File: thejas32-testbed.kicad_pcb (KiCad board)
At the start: 4 copper layers, 141.5 x 110 mm, 98 parts, among them J1 Conn_02x04_Odd_Even, J10 Conn_02x10_Odd_Even, J11 Conn_02x03_Odd_Even, J12 Conn_02x20_Odd_Even, J13 Conn_02x06_Odd_Even, J2 USB_B_Micro, J3 Conn_02x03_Odd_Even, J4 Conn_02x04_Odd_Even, J6 Conn_02x06_Odd_Even, J7 Conn_01x05, U1 Pico Master, U2 THEJAS32, U3 Pico Slave, U6 W25Q16JVSSIQ

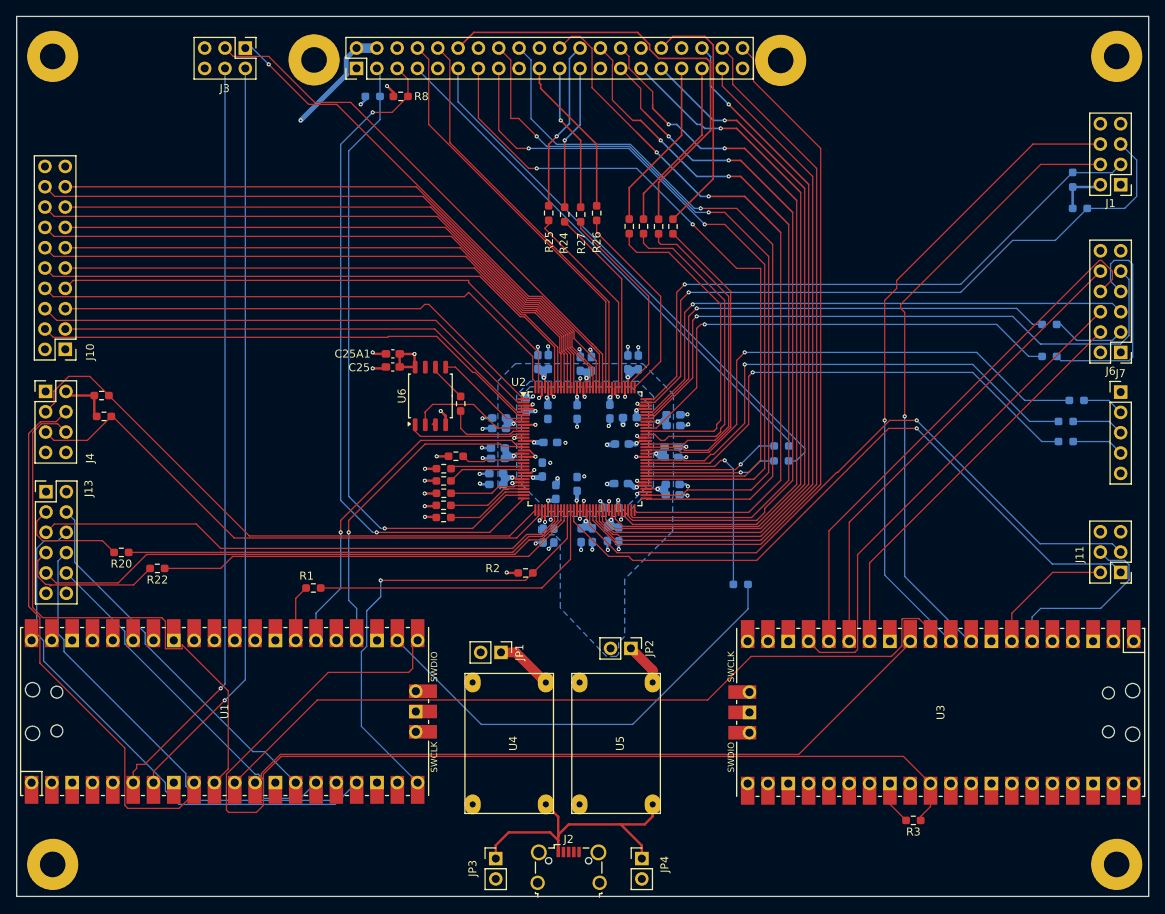
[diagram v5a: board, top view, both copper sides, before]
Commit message: Nicely routed PCB, clean lines
Reasonable spacing between traces. Could be improved.
Done for testing mostly.
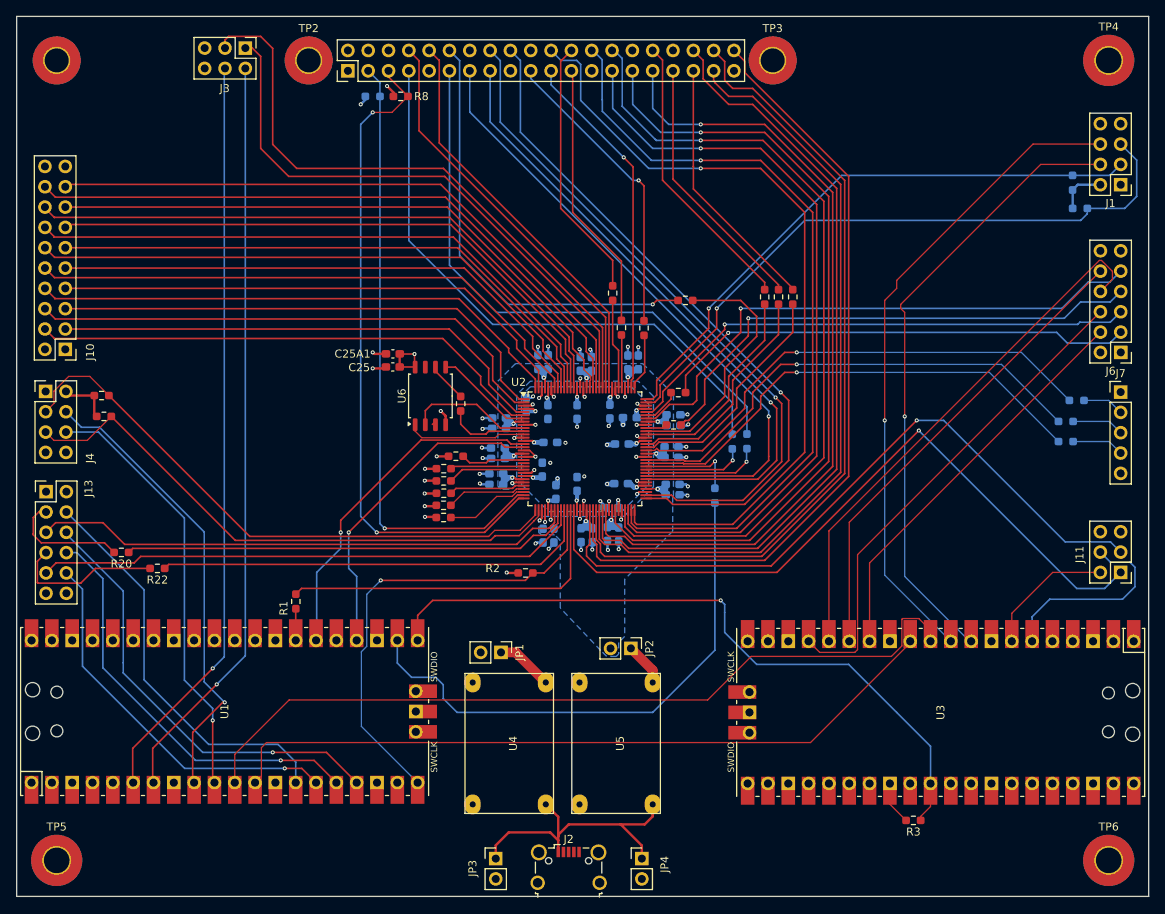
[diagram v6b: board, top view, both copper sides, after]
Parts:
- removed R27: 0E, project_lib:proj_R_0603_1608Metric_Pad0.98x0.95mm_HandSolder
- R16, R18: moved to F.Cu
- TP1, TP2, TP3: footprint MountingHole:MountingHole_3.2mm_M3_Pad -> MountingHole:MountingHole_3mm_Pad_TopBottom
- TP4, TP5, TP6: footprint MountingHole:MountingHole_3.2mm_M3_Pad -> MountingHole:MountingHole_3.2mm_M3_Pad_TopBottom
- moved TP1 166.3 mm to (89.5, 55.5)
- moved TP6 108.1 mm to (221.0, 155.5)
- moved TP2 105.5 mm to (121.0, 55.5)
- moved TP5 105.1 mm to (89.5, 155.5)
- moved TP3 90.0 mm to (179.0, 55.5)
- moved R18 47.7 mm to (166.6, 101.1)
- moved R16 47.2 mm to (167.2, 97.0)
- moved R29 17.5 mm to (178.0, 85.1)
- moved R30 17.4 mm to (179.7, 85.1)
- moved R31 17.4 mm to (181.5, 85.1)
- moved R24 15.8 mm to (160.1, 88.9)
- moved R26 15.5 mm to (162.9, 89.0)
- moved R25 12.8 mm to (159.0, 84.6)
- moved R28 11.6 mm to (168.1, 85.5), turned to 180 degrees
- moved R35 11.6 mm to (171.8, 109.9), turned to -90 degrees
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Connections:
- R28 pad 2: RPi_COMPAT_PWM1 -> RPi_COMPAT_PWM0
- R29 pad 2: RPi_COMPAT_PWM1_ALT -> RPi_COMPAT_PWM0_ALT
- R30 pad 2: RPi_COMPAT_PWM0 -> RPi_COMPAT_PWM1
- R31 pad 2: RPi_COMPAT_PWM0_ALT -> RPi_COMPAT_PWM1_ALT
- U2 pad 98: Net-(U2-SPI2_MISO) -> RPi_COMPAT_SPI0_MISO
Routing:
- net Net-(U2-SPI0_MOSI): track 60.8 -> 2.67 mm, vias 1 -> 0
- net Net-(U2-SPIO0_CLK): track 60.4 -> 4.76 mm, vias 1 -> 0
- net Net-(J6-Pin_3): track 9.27 -> 59.9 mm, vias 0 -> 1
- net PICO_SLAVE_RUN: track 136.8 -> 87.4 mm, vias 0 -> 1
- net Net-(J6-Pin_7): track 28.6 -> 65.0 mm, vias 0 -> 1
- net RPi_COMPAT_SPI0_MISO: track 18.4 -> 44.7 mm
- net Net-(U2-SPI2_MISO): track 25.1 -> 0.00 mm
- net Net-(U2-SPI2_MOSI): track 26.1 -> 8.31 mm
- net RPi_COMPAT_SPI0_MOSI: track 20.1 -> 37.5 mm, vias 0 -> 1
- net Net-(U2-SPI2_CLK): track 23.7 -> 6.58 mm
- net MCU_I2C0_SDA: track 70.6 -> 53.9 mm, vias 0 -> 1
- net RPi_COMPAT_SPI0_SCLK: track 18.1 -> 33.8 mm, vias 1 -> 0
- net Net-(U2-PWM1): track 41.0 -> 25.9 mm
- net Net-(U2-PWM7): track 26.1 -> 12.2 mm
- net Net-(U2-SPI2_CSN): track 24.9 -> 11.2 mm
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
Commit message: Single pico, new layout
Figured two picos was too much as a concept. So, simplify.

Reduce number of jumpers etc also (especially in passthrough).

The single pico breaks out pins conveniently for users for
usage.
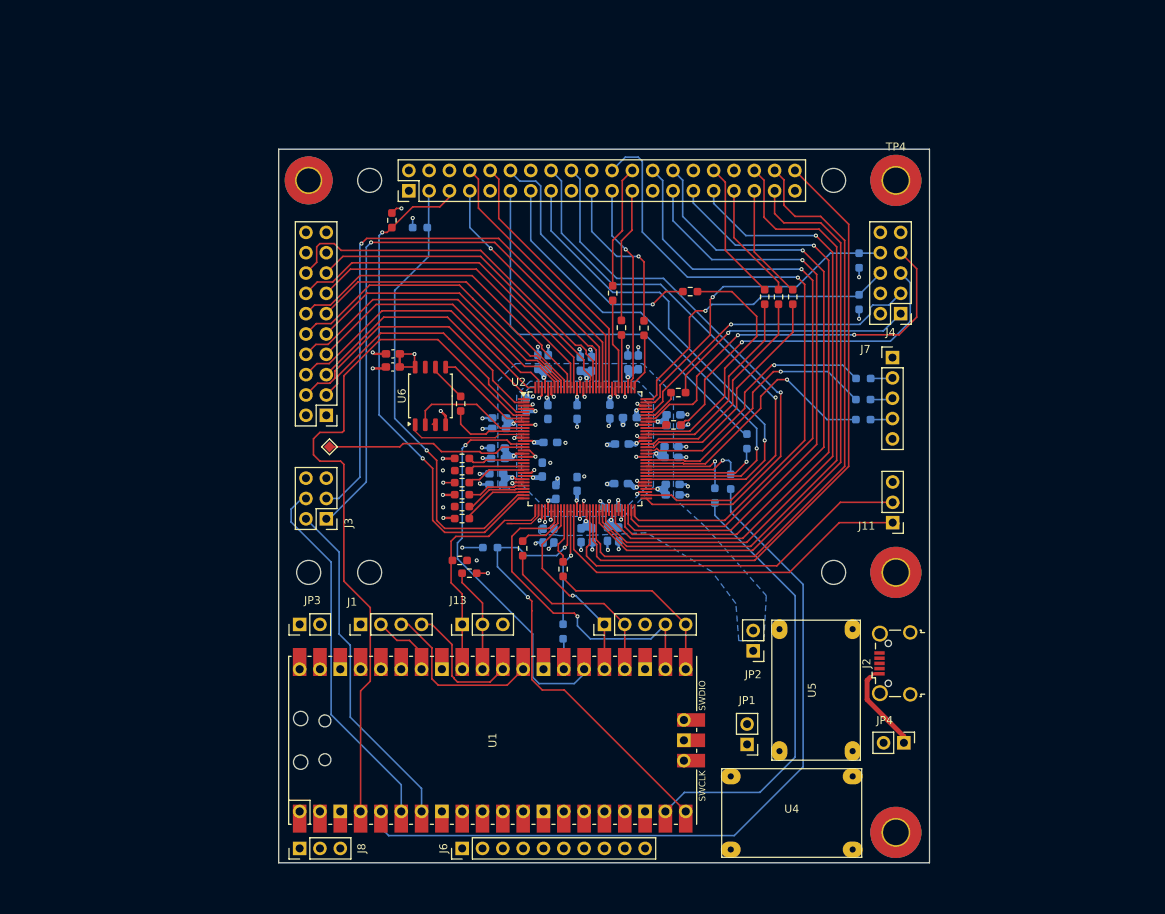
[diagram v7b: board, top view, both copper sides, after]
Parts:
- removed R3: 10K, project_lib:proj_R_0603_1608Metric_Pad0.98x0.95mm_HandSolder
- removed TP3: Mounting Hole, MountingHole:MountingHole_3mm_Pad_TopBottom
- removed TP5: Mounting Hole, MountingHole:MountingHole_3.2mm_M3_Pad_TopBottom
- removed U3: Pico Slave, RPi_Pico:RPi_Pico_SMD_TH
- added H1: MountingHole, MountingHole:MountingHole_3mm, F.Cu at (128.6, 70.5)
- added H2: MountingHole, MountingHole:MountingHole_3mm, F.Cu at (186.6, 70.5)
- added H3: MountingHole, MountingHole:MountingHole_3mm, F.Cu at (128.6, 119.5)
- added H4: MountingHole, MountingHole:MountingHole_3mm, F.Cu at (186.6, 119.5)
- added H5: MountingHole, MountingHole:MountingHole_3mm, F.Cu at (121.0, 119.5)
- added J8: Conn_01x03, Connector_PinHeader_2.54mm:PinHeader_1x03_P2.54mm_Vertical, F.Cu at (119.9, 154.0)
- added J9: Conn_01x05, Connector_PinHeader_2.54mm:PinHeader_1x05_P2.54mm_Vertical, F.Cu at (158.0, 126.0)
- added TP7: TestPoint, TestPoint:TestPoint_Pad_1.0x1.0mm, F.Cu at (123.6, 103.8)
- J1: value Conn_02x04_Odd_Even -> Conn_01x04; footprint Connector_PinHeader_2.54mm:PinHeader_2x04_P2.54mm_Vertical -> Connector_PinHeader_2.54mm:PinHeader_1x04_P2.54mm_Vertical
- J11: value Conn_02x03_Odd_Even -> Conn_01x03; footprint Connector_PinHeader_2.54mm:PinHeader_2x03_P2.54mm_Vertical -> Connector_PinHeader_2.54mm:PinHeader_1x03_P2.54mm_Vertical
- J13: value Conn_02x06_Odd_Even -> Conn_01x03; footprint Connector_PinHeader_2.54mm:PinHeader_2x06_P2.54mm_Vertical -> Connector_PinHeader_2.54mm:PinHeader_1x03_P2.54mm_Vertical
- J4: value Conn_02x04_Odd_Even -> Conn_02x05_Odd_Even; footprint Connector_PinHeader_2.54mm:PinHeader_2x04_P2.54mm_Vertical -> Connector_PinHeader_2.54mm:PinHeader_2x05_P2.54mm_Vertical
- J6: value Conn_02x06_Odd_Even -> Conn_01x10; footprint Connector_PinHeader_2.54mm:PinHeader_2x06_P2.54mm_Vertical -> Connector_PinHeader_2.54mm:PinHeader_1x10_P2.54mm_Vertical
- R1, R2: moved to B.Cu
- TP2: footprint MountingHole:MountingHole_3mm_Pad_TopBottom -> MountingHole:MountingHole_3.2mm_M3_Pad_TopBottom
- moved TP2 121.2 mm to (194.4, 152.0)
- moved J1 109.8 mm to (127.5, 126.0), turned to 90 degrees
- moved J4 107.3 mm to (195.0, 87.2), turned to 180 degrees
- moved J6 103.1 mm to (140.2, 154.0), turned to 90 degrees
- moved J3 59.7 mm to (123.2, 112.8), turned to 180 degrees
- moved J13 54.6 mm to (140.2, 126.0), turned to 90 degrees
- moved R22 50.7 mm to (152.8, 119.1), turned to -90 degrees
- moved R20 50.2 mm to (147.8, 116.5), turned to -90 degrees
- moved R5 49.7 mm to (141.1, 119.6), turned to 180 degrees
- moved R4 49.3 mm to (139.9, 118.0), turned to 180 degrees
- moved J2 48.1 mm to (194.2, 130.9), turned to 90 degrees
- moved TP6 44.8 mm to (194.4, 119.5)
- moved JP3 38.2 mm to (119.9, 126.0), turned to 90 degrees
- moved U4 36.4 mm to (181.4, 149.6), turned to 180 degrees
- moved JP4 35.8 mm to (195.4, 140.8), turned to -90 degrees
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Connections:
- J1 pad 1: PWR_3V3 -> GND
- J1 pad 2: PWR_3V3 -> Net-(J1-Pin_2)
- J1 pad 4: MCU_I2C1_SCL -> Net-(J1-Pin_4)
- J10 pad 10: MCU_GPIO_22 -> MCU_GPIO_24
- J10 pad 12: MCU_GPIO_24 -> MCU_GPIO_26
- J10 pad 14: MCU_GPIO_26 -> MCU_GPIO_28
- J10 pad 16: MCU_GPIO_28 -> MCU_GPIO_30
- J10 pad 17: MCU_GPIO_31 -> unconnected-(J10-Pin_17-Pad17)
- J10 pad 18: MCU_GPIO_30 -> unconnected-(J10-Pin_18-Pad18)
- J10 pad 4: MCU_GPIO_16 -> MCU_GPIO_18
- J10 pad 6: MCU_GPIO_18 -> MCU_GPIO_20
- J10 pad 8: MCU_GPIO_20 -> MCU_GPIO_22
- J11 pad 2: MCU_UART1_TX -> Net-(J11-Pin_2)
- J11 pad 3: Net-(J11-Pin_3) -> GND
- J13 pad 1: PWR_3V3 -> MCU_I2C0_SCL
- J13 pad 2: PWR_3V3 -> MCU_I2C0_SDA
- J13 pad 3: Net-(J13-Pin_3) -> GND
- J2 pad 1: PWR_5V -> Net-(J2-VBUS)
- J4 pad 1: PWR_3V3 -> MCU_SPI0_SCK
- J4 pad 3: Net-(J4-Pin_3) -> MCU_SPI0_CSN
- J4 pad 4: MCU_I2C0_SCL -> PWR_3V3
- J4 pad 5: Net-(J4-Pin_5) -> MCU_SPI0_MOSI
- J4 pad 6: MCU_I2C0_SDA -> MCU_I2C1_SCL
- J4 pad 7: GND -> MCU_SPI0_MISO
- J4 pad 8: GND -> MCU_I2C1_SDA
- J6 pad 1: PWR_3V3 -> Net-(J6-Pin_1)
- J6 pad 10: MCU_SPI0_MISO -> GND
- J6 pad 2: PWR_3V3 -> Net-(J6-Pin_2)
- J6 pad 4: MCU_SPI0_SCK -> Net-(J6-Pin_4)
- J6 pad 5: Net-(J6-Pin_5) -> GND
- J6 pad 6: MCU_SPI0_CSN -> Net-(J6-Pin_6)
- J6 pad 8: MCU_SPI0_MOSI -> Net-(J6-Pin_8)
- JP4 pad 1: PWR_5V -> Net-(J2-VBUS)
- JP4 pad 2: Net-(JP4-B) -> PWR_5V
- R16 pad 2: Net-(J6-Pin_3) -> MCU_SPI0_SCK
- R18 pad 2: Net-(J6-Pin_7) -> MCU_SPI0_MOSI
- R20 pad 2: Net-(J13-Pin_3) -> MCU_SPI1_SCK
- R22 pad 2: Net-(J13-Pin_7) -> MCU_SPI1_MOSI
- R36 pad 2: RPi_COMPAT_GPIO_4 -> MCU_GPIO_00
- R4 pad 2: Net-(J4-Pin_3) -> MCU_I2C0_SCL
- R5 pad 2: Net-(J4-Pin_5) -> MCU_I2C0_SDA
- R6 pad 2: Net-(J1-Pin_3) -> MCU_I2C1_SCL
- R7 pad 2: Net-(J1-Pin_5) -> MCU_I2C1_SDA
- U1 pad 1: unconnected-(U1-GPIO0-Pad1)_0 -> Net-(J8-Pin_1)
- U1 pad 10: MCU_I2C0_SDA -> Net-(J6-Pin_2)
- U1 pad 11: PICO_COMM_1 -> Net-(J6-Pin_3)
- U1 pad 12: PICO_COMM_2 -> Net-(J6-Pin_4)
- U1 pad 14: MCU_SPI1_SCK -> Net-(J6-Pin_6)
- U1 pad 15: MCU_SPI1_MISO -> Net-(J6-Pin_7)
- U1 pad 16: MCU_SPI1_MOSI -> Net-(J6-Pin_8)
- U1 pad 17: MCU_SPI1_CSN -> Net-(J6-Pin_9)
- U1 pad 19: unconnected-(U1-GPIO14-Pad19)_0 -> MCU_PWM_7
- U1 pad 2: unconnected-(U1-GPIO1-Pad2) -> Net-(J8-Pin_2)
- U1 pad 21: PICO_SLAVE_RUN -> MCU_SPI1_MOSI
- U1 pad 22: MCU_PWM_7 -> MCU_SPI1_CSN
- U1 pad 24: MCU_HEART_BEAT -> MCU_SPI1_SCK
- U1 pad 25: unconnected-(U1-GPIO19-Pad25) -> MCU_SPI1_MISO
- U1 pad 29: unconnected-(U1-GPIO22-Pad29) -> Net-(J1-Pin_3)
- U1 pad 30: unconnected-(U1-RUN-Pad30) -> Net-(J1-Pin_4)
- U1 pad 31: unconnected-(U1-GPIO26_ADC0-Pad31)_0 -> MCU_I2C0_SDA
- U1 pad 32: unconnected-(U1-GPIO27_ADC1-Pad32)_0 -> MCU_I2C0_SCL
- U1 pad 34: unconnected-(U1-GPIO28_ADC2-Pad34)_0 -> Net-(J1-Pin_2)
- U1 pad 4: unconnected-(U1-GPIO2-Pad4)_0 -> MCU_GPIO_16
- U1 pad 5: unconnected-(U1-GPIO3-Pad5) -> MCU_GPIO_00
- U1 pad 9: MCU_I2C0_SCL -> Net-(J6-Pin_1)
- U2 pad 109: MCU_GPIO_31 -> RPi_COMPAT_GPIO_4
- U2 pad 16: MCU_HEART_BEAT -> Net-(U2-PROC_HEART_BEAT)
- U2 pad 33: Net-(J4-Pin_3) -> MCU_I2C0_SCL
- U2 pad 34: Net-(J4-Pin_5) -> MCU_I2C0_SDA
- U2 pad 39: Net-(J13-Pin_5) -> MCU_SPI1_CSN
- U2 pad 41: Net-(J13-Pin_9) -> MCU_SPI1_MISO
- U2 pad 50: Net-(J11-Pin_3) -> Net-(J11-Pin_2)
- U2 pad 90: Net-(J6-Pin_9) -> MCU_SPI0_MISO
- U2 pad 92: Net-(J6-Pin_5) -> MCU_SPI0_CSN
- U2 pad 95: Net-(J1-Pin_5) -> MCU_I2C1_SDA
- U2 pad 96: Net-(J1-Pin_3) -> MCU_I2C1_SCL
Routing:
- net PWR_3V3: track 467.5 -> 226.3 mm, vias 15 -> 19
- net PICO_COMM_1: track 101.5 -> 0.00 mm
- net MCU_GPIO_00: track 0.00 -> 97.3 mm
- net PICO_COMM_2: track 91.4 -> 0.00 mm
- net Net-(J11-Pin_3): track 87.5 -> 0.00 mm, vias 1 -> 0
- net PICO_SLAVE_RUN: track 87.4 -> 0.00 mm, vias 1 -> 0
- net Net-(J1-Pin_5): track 82.1 -> 0.00 mm, vias 1 -> 0
- net MCU_GPIO_31: track 80.5 -> 0.00 mm
- net Net-(J4-Pin_3): track 74.5 -> 0.00 mm
- net Net-(J4-Pin_5): track 71.7 -> 0.00 mm
- net Net-(J6-Pin_9): track 70.5 -> 0.00 mm, vias 1 -> 0
- net Net-(J13-Pin_9): track 68.7 -> 0.00 mm
- net Net-(J13-Pin_5): track 67.9 -> 0.00 mm
- net Net-(JP3-B): track 73.6 -> 6.65 mm
- net Net-(JP4-B): track 66.4 -> 0.00 mm
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- added copper zone on In2.Cu, net PWR_5V
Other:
- board size 141.5 x 110 mm -> 81.4 x 89.2 mm
- board text added: "${REFERENCE}"

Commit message: Incorporated most review comments.
Used 5 mils traces in breakout area. This results in very few DRC
errors iff track spacing is set to 5 mils.  However, setting it to
8 mils (in board settings) does complain essentially for every pad
of the THEJAS32. Those just need to be waived off.

Ensure 16 mils track separation, except in breakout area. This can
be verified by setting the track spacing to 16 mils and running the
DRC. Except for the core area, and some issues on the USB connector,
no other errors must pop up.

Poured copper on every layer. Added GND vias to increase GND pour.

Moved flash IC to improve routing to the GPIO connector.

Moved USB connector close to the RP2040s USB connector, J3 placed
next to it. So both jumpers are now close.

Added MPN field, and populated it for many components, except caps
and headers.

Pending: Power nets are routed at 12 mils from THEJAS32. Get it down
to 5 mil ?
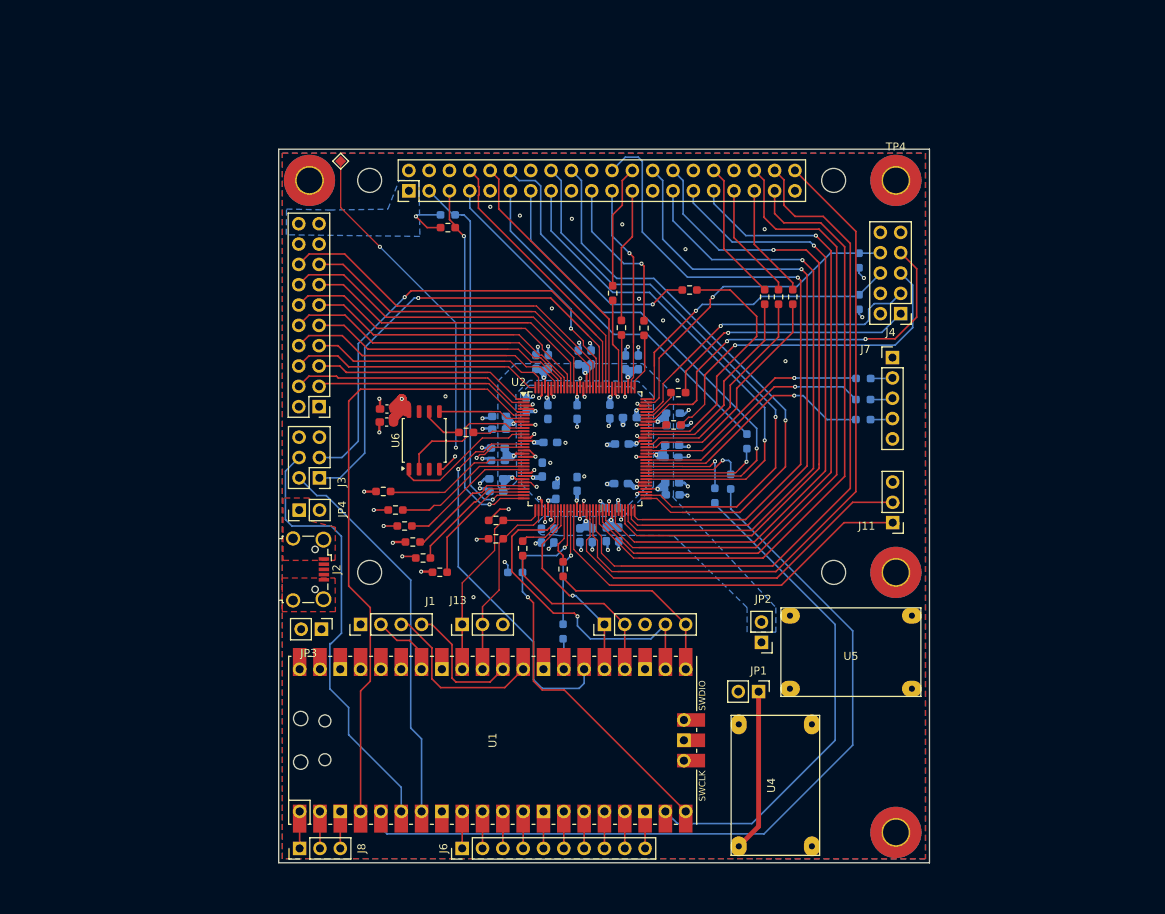
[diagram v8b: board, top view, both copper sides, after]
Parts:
- removed H5: MountingHole, MountingHole:MountingHole_3mm
- R1, R16, R18, R20, R22, R24, R25, R26, R28, R29, R30, R31, R32, R33, R34, R35, R36, R37, R70: value 0E -> 27E
- TP1: footprint MountingHole:MountingHole_3mm_Pad_TopBottom -> MountingHole:MountingHole_3.2mm_M3_Pad_TopBottom
- moved JP4 81.0 mm to (119.8, 111.7), turned to 90 degrees
- moved J2 74.2 mm to (121.0, 119.1), turned to -90 degrees
- moved TP7 35.7 mm to (125.0, 68.1)
- moved R38 10.7 mm to (130.3, 109.4)
- moved R39 9.67 mm to (131.9, 111.7)
- moved R40 9.00 mm to (133.0, 113.7)
- moved R41 8.54 mm to (134.0, 115.7)
- moved R42 8.07 mm to (135.3, 117.7)
- moved R43 7.26 mm to (137.4, 119.5)
- moved R8 7.06 mm to (138.4, 76.4), turned to 0 degrees
- moved C25A1 6.93 mm to (130.8, 99.1)
- moved C25 6.92 mm to (130.7, 100.7)
- moved JP1 6.76 mm to (177.2, 134.4), turned to -90 degrees
- moved R4 6.74 mm to (144.4, 113.0), turned to 0 degrees
- moved U5 6.45 mm to (188.8, 129.5), turned to 0 degrees
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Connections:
- J10 pad 1: PWR_3V3 -> GND
- J10 pad 19: GND -> PWR_3V3
- J10 pad 2: PWR_3V3 -> GND
- J10 pad 20: GND -> PWR_3V3
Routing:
- net PWR_5V: track 188.1 -> 136.5 mm
- net PWR_3V3: track 226.3 -> 185.8 mm, vias 19 -> 18
- net Net-(U2-PROC_HEART_BEAT): track 25.2 -> 51.3 mm, vias 0 -> 3
- net GND: track 79.8 -> 98.6 mm, vias 69 -> 82
- net RPi_COMPAT_I2C1_SCL: track 64.3 -> 47.1 mm
- net Net-(J3-Pin_3): track 76.0 -> 59.5 mm
- net Net-(J3-Pin_1): track 76.1 -> 59.7 mm
- net Net-(JP1-A): track 4.84 -> 20.4 mm
- net MCU_GPIO_16: track 90.9 -> 76.8 mm
- net Net-(J2-VBUS): track 11.6 -> 0.00 mm
- net MCU_TST_CLK: track 7.12 -> 18.4 mm
- net RPi_COMPAT_I2C1_SDA: track 58.2 -> 47.4 mm
- net MCU_TJTAG_TMS: track 7.52 -> 17.4 mm
- net MCU_BOOT_UART_RX: track 45.9 -> 55.1 mm
- net MCU_TJTAG_TDI: track 7.98 -> 16.9 mm
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- added copper zone on F.Cu, net GND
- added copper zone on In2.Cu, net GND
- added copper zone on F.Cu, net Net-(J2-VBUS)
- added copper zone on B.Cu, net PWR_3V3
- removed copper zone on In1.Cu, net GND
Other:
- board text removed: "${REFERENCE}"
